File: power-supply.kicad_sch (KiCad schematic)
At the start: 17 parts

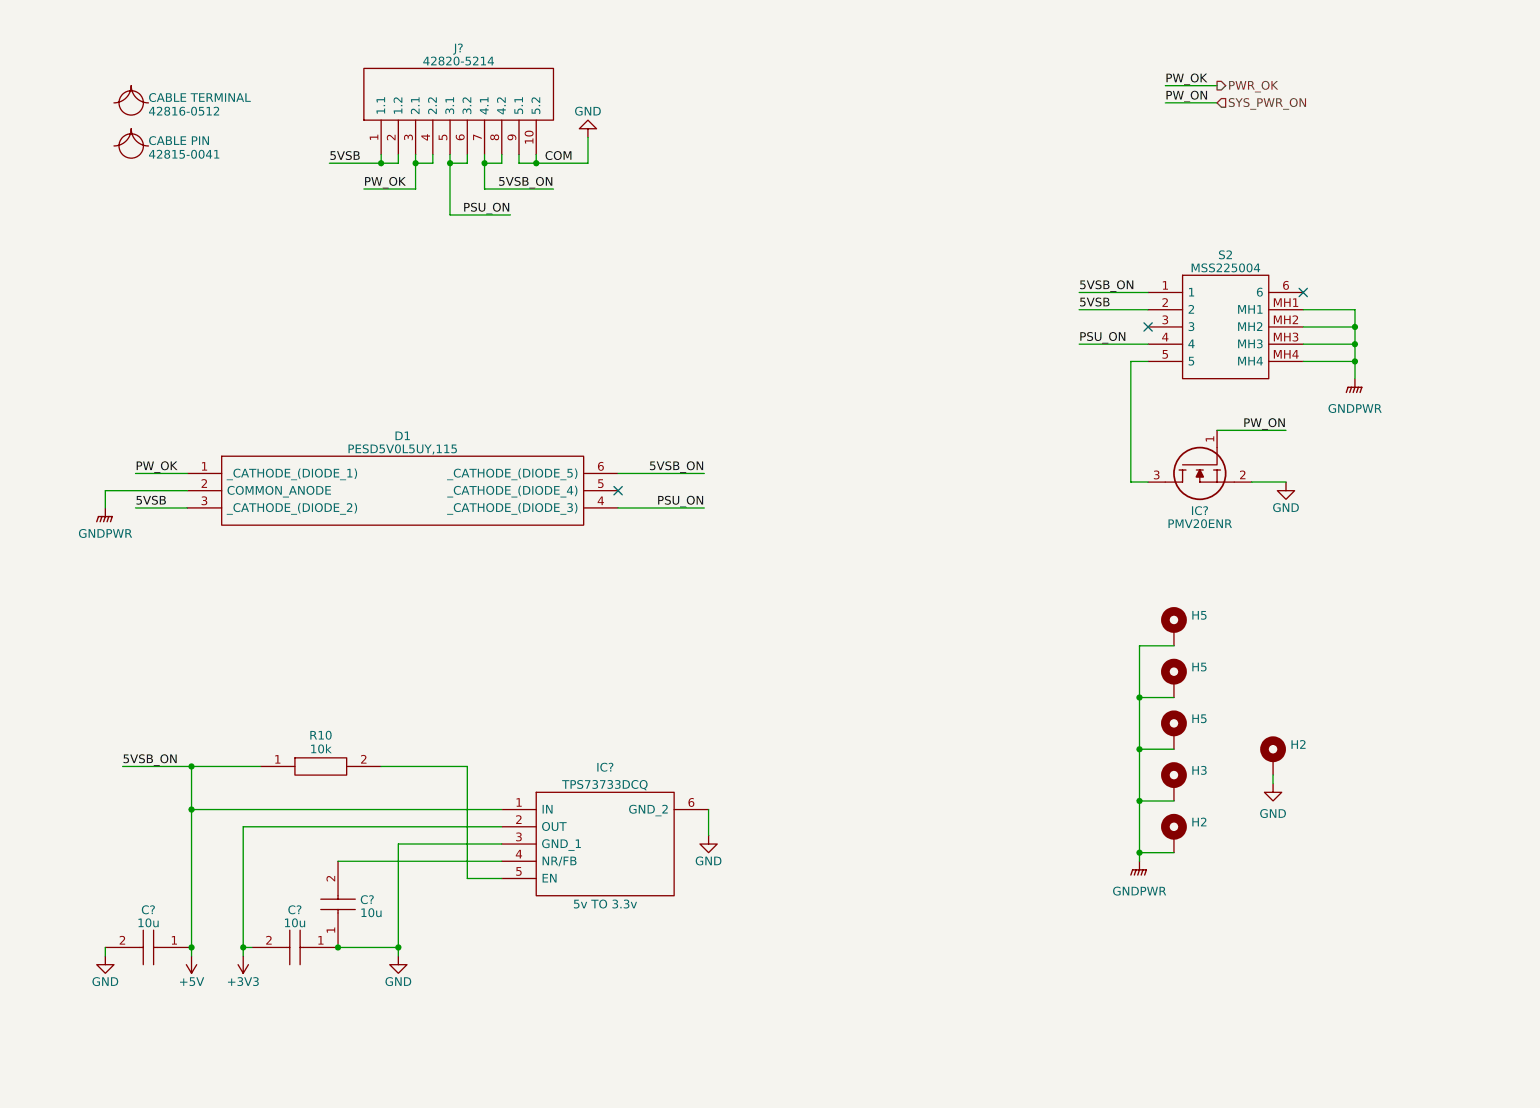
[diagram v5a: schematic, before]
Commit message: improve ESD, net classes and power diodes
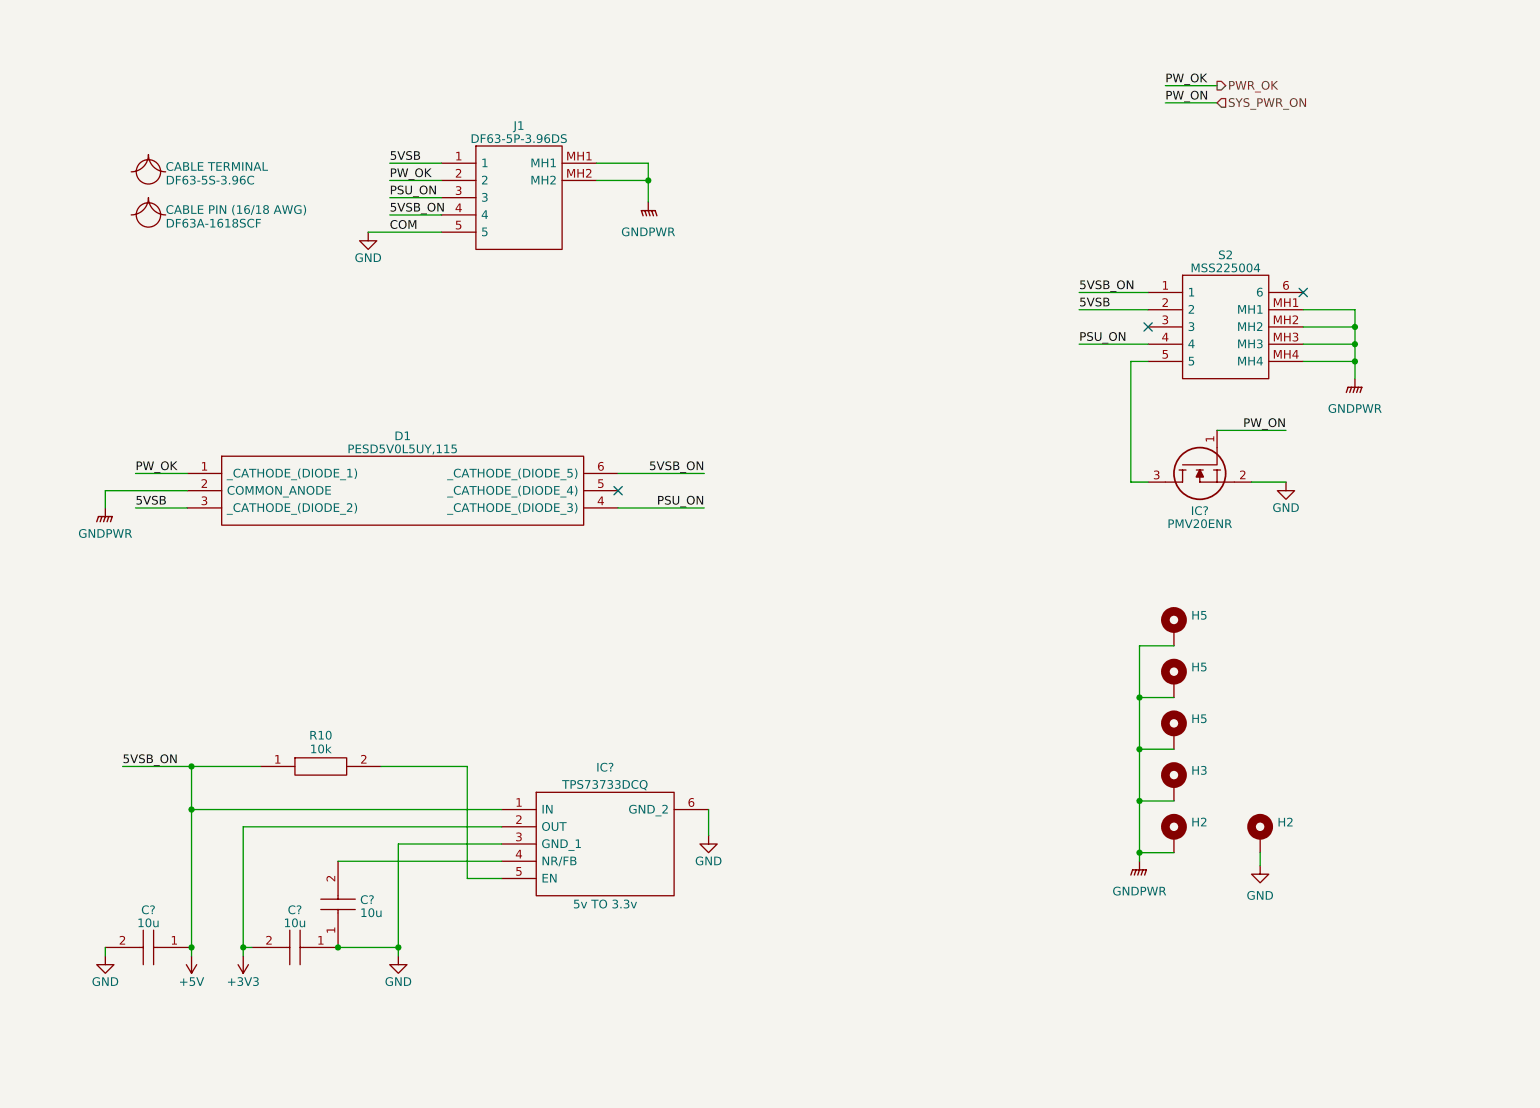
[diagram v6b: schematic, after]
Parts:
- removed J?: 42820-5214, 42820-5XXY_1, symbol SamacSys_Parts:42820-5223
- added J1: DF63-5P-3.96DS, DF635P396DS, symbol SamacSys_Parts:DF63-5P-3.96DS
- B?: value 42816-0512 -> DF63-5S-3.96C; Manufacturer_Part_Number 42816-0512 -> DF63-5S-3.96C; Mouser Part Number 538-42816-0512 -> 798-DF63-5S-3.96C
- B?: value 42815-0041 -> DF63A-1618SCF; Manufacturer_Part_Number 42815-0041 (Loose Piece) -> DF63A-1618SCF; Mouser Part Number 538-42815-0041-LP -> 798-DF63A-1618SCF; Note CABLE PIN -> CABLE PIN (16/18 AWG)
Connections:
- net +5V: now also J1.4
- net 5VSB: now also J1.1
- net GND: now also J1.5
- net GNDPWR: now also J1.MH1, J1.MH2
- net PSU_ON: now also J1.3
- net PWR_OK: now also J1.2
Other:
- moved on the sheet: H2

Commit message: initial component layout
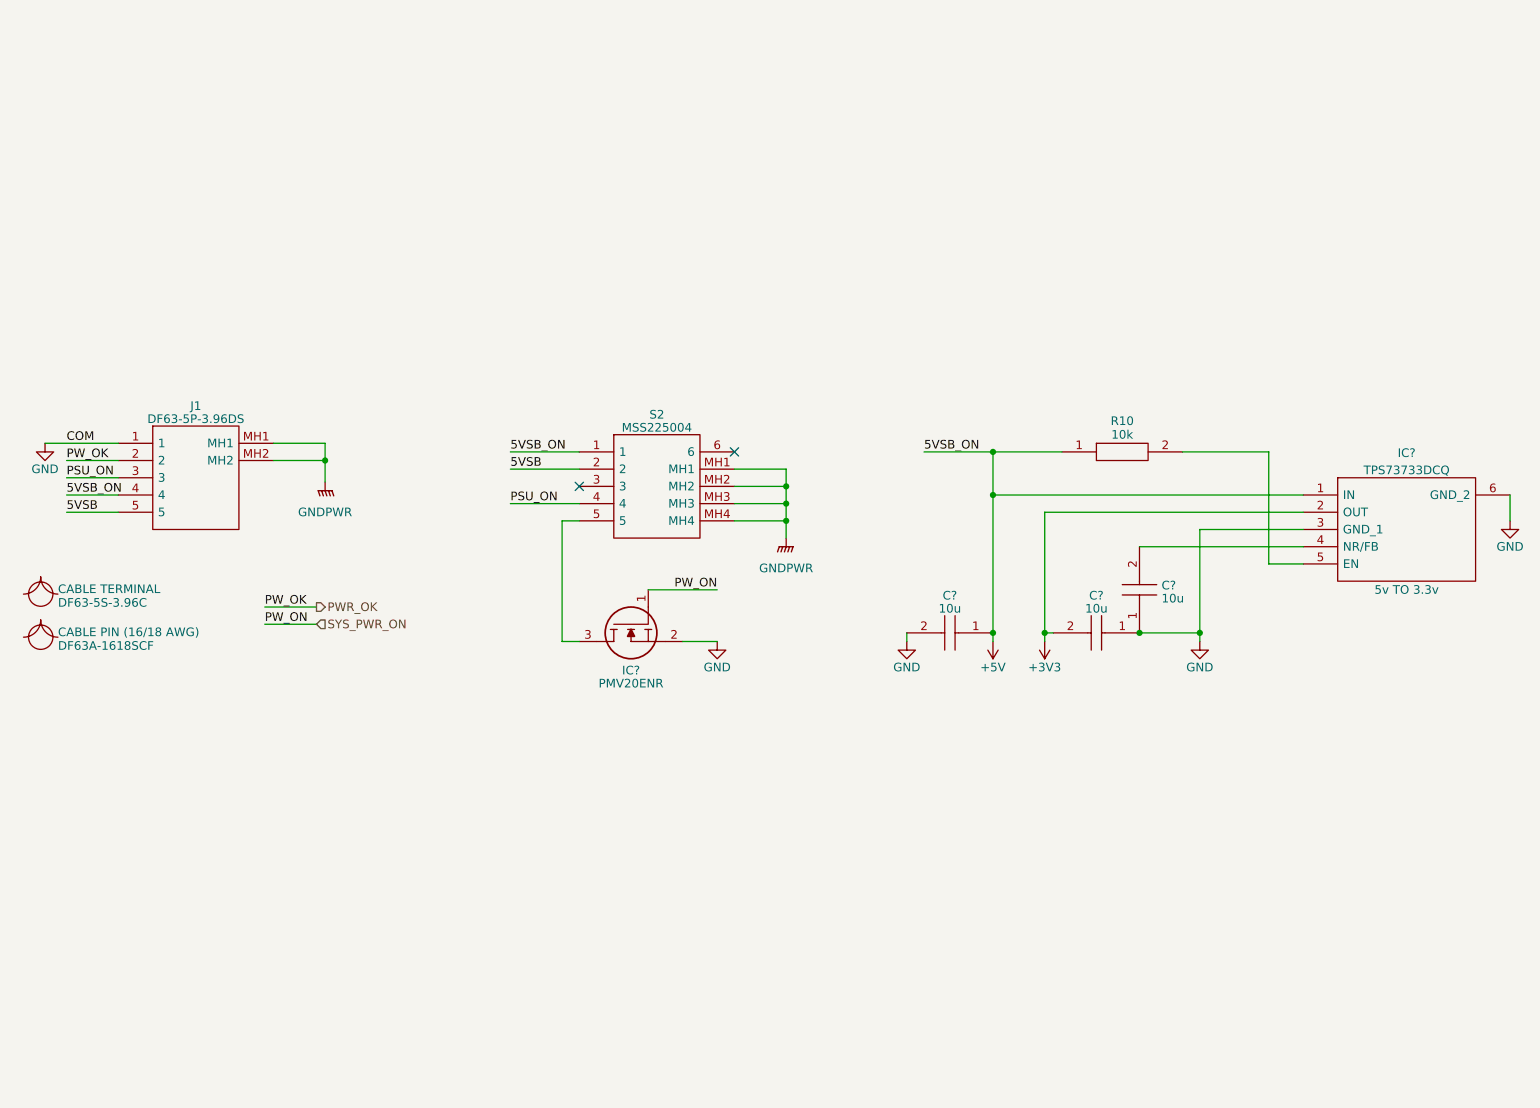
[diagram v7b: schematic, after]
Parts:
- removed D1: PESD5V0L5UY,115, PESD5V0L5UY115, symbol SamacSys_Parts:PESD5V0L5UY,115
- removed H2 (x2), H3, H5 (x3): MountingHole_Pad, MountingHole:MountingHole_3.2mm_M3_Pad_Via, symbol Mechanical:MountingHole_Pad
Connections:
- net 5VSB: now also J1.5; no longer J1.1
- net GND: now also J1.1; no longer J1.5
- no-connect marks 3 -> 2
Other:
- moved on the sheet: C?, IC?, J1, R10, S2
